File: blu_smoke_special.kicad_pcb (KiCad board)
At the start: 2 copper layers, 50.8 x 25.4 mm, 35 parts, among them P1 MOLEX-8981, P2 CONN_1, P3 CONN_1, Q1 2N3904, U1 555

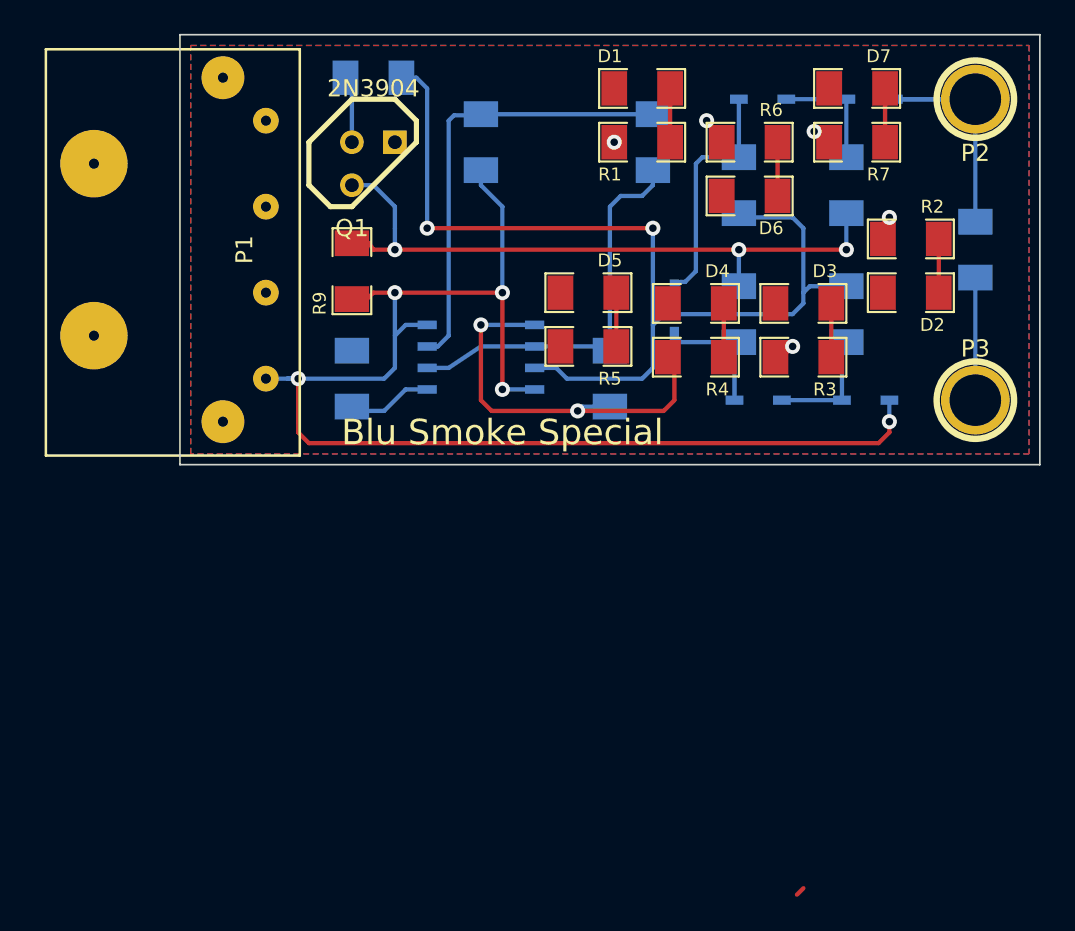
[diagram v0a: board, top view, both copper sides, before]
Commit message: Added a switch.
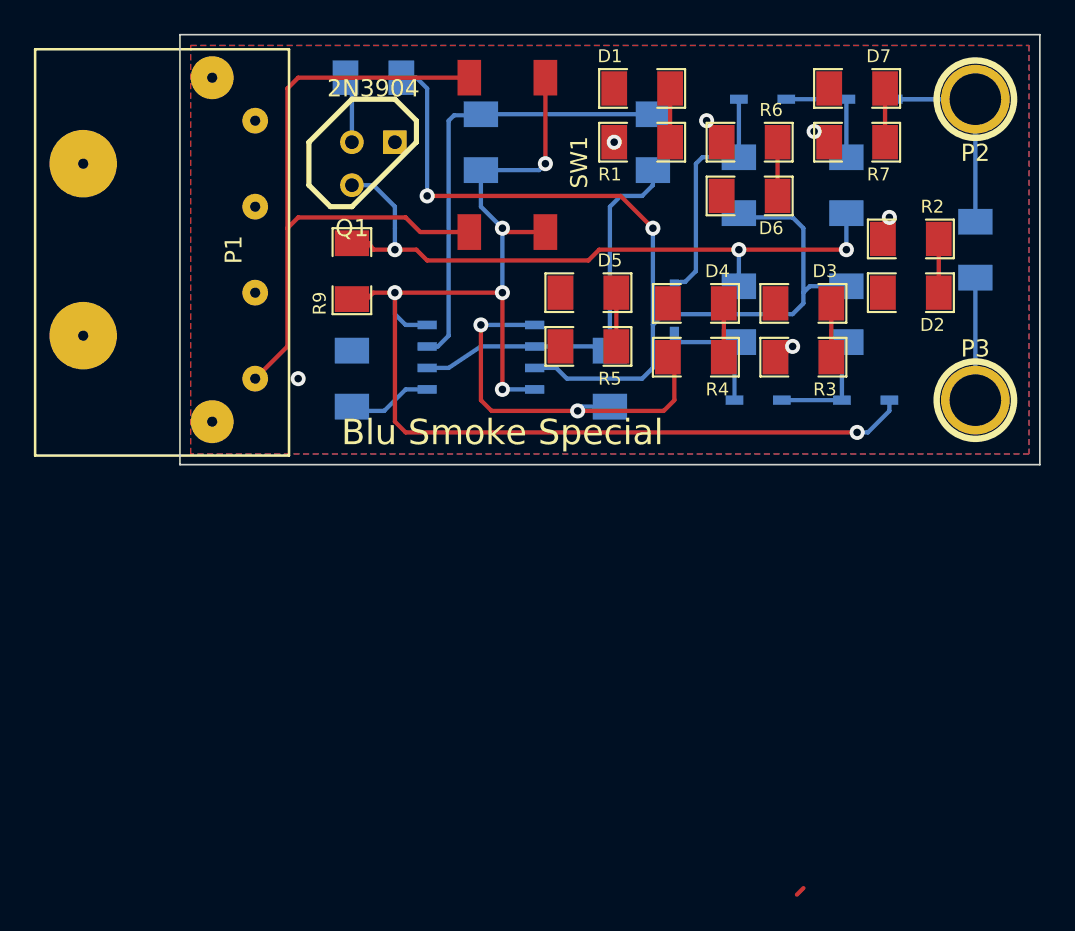
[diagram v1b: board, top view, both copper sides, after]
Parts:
- added SW1: FSM4JSMA, FSM4JSMA, F.Cu at (104.1, 115.6)
- moved P1 0.63 mm to (87.0, 135.9)
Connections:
- C2 pad 2: N-000005 (its old number) -> /CLK1
- C4 pad 2: N-000005 (its old number) -> /CLK1
- C5 pad 1: /CLK1 -> /HV
- D13 pad 2: /CLK1 -> /HV
- P1 pad 1: /PWR -> N-0000016
- P2 pad 1: /CLK1 -> /HV
- Q1 pad 3: N-000005 (its old number) -> /CLK1
- R9 pad 2: N-000005 (its old number) -> /CLK1
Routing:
- net N-0000016: track 0.00 -> 40.3 mm
- net N-000005 (its old number): track 39.3 -> 0.00 mm, vias 3 -> 0
- net /CLK1: track 15.6 -> 39.9 mm, vias 0 -> 3
- net /HV: track 0.00 -> 15.6 mm
- net /PWR: track 80.1 -> 77.8 mm, vias 5 -> 6
- net /CLK0: track 60.4 -> 59.3 mm
- net (no net): vias 0 -> 1
